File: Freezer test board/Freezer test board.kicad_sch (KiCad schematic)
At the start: 18 parts, among them J1 TB007-508-03BE, J2 TB007-508-03BE, J3 TB007-508-03BE, J4 TB007-508-03BE, J5 TB007-508-03BE, J6 TB007-508-03BE, J7 Conn_02x20_Odd_Even, J8 Conn_02x02_Odd_Even

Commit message: temp commit
I just curved the edges of the PCB and un-did all the connection
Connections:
- no-connect marks 0 -> 5
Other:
- moved on the sheet: H1, H2, H4
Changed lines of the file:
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@@
 		)
+	)
+	(no_connect
+		(at 113.03 78.74)
+	)
+	(no_connect
+		(at 118.11 77.47)
+	)
+	(no_connect
+		(at 107.95 80.01)
+	)
+	(no_connect
+		(at 109.22 77.47)
+	)
+	(no_connect
+		(at 118.11 80.01)
 	)
 	(wire
@@
 	(symbol
 		(lib_id "Mechanical:MountingHole")
-		(at 106.68 38.1 0)
+		(at 106.68 40.64 0)
 		(unit 1)
 		(exclude_from_sim no)
@@
 		(fields_autoplaced yes)
 		(property "Reference" "H4"
-			(at 109.22 36.8299 0)
+			(at 109.22 39.3699 0)
 			(effects
 				(font
@@
 		)
 		(property "Value" "MountingHole"
-			(at 109.22 39.3699 0)
+			(at 109.22 41.9099 0)
 			(effects
 				(font
@@
 		)
 		(property "Footprint" "MountingHole:MountingHole_2.5mm_Pad"
-			(at 106.68 38.1 0)
+			(at 106.68 40.64 0)
 			(effects
 				(font
@@
 		)
 		(property "Datasheet" "~"
-			(at 106.68 38.1 0)
+			(at 106.68 40.64 0)
 			(effects
 				(font
@@
 		)
 		(property "Description" "Mounting Hole without connection"
-			(at 106.68 38.1 0)
+			(at 106.68 40.64 0)
 			(effects
 				(font
@@
 	(symbol
 		(lib_id "Mechanical:MountingHole")
-		(at 85.09 31.75 0)
+		(at 85.09 30.48 0)
 		(unit 1)
 		(exclude_from_sim no)
@@
 		(fields_autoplaced yes)
 		(property "Reference" "H1"
-			(at 87.63 30.4799 0)
+			(at 87.63 29.2099 0)
 			(effects
 				(font
@@
 		)
 		(property "Value" "MountingHole"
-			(at 87.63 33.0199 0)
+			(at 87.63 31.7499 0)
 			(effects
 				(font
@@
 		)
 		(property "Footprint" "MountingHole:MountingHole_2.5mm_Pad"
-			(at 85.09 31.75 0)
+			(at 85.09 30.48 0)
 			(effects
 				(font
@@
 		)
 		(property "Datasheet" "~"
-			(at 85.09 31.75 0)
+			(at 85.09 30.48 0)
 			(effects
 				(font
@@
 		)
 		(property "Description" "Mounting Hole without connection"
-			(at 85.09 31.75 0)
+			(at 85.09 30.48 0)
 			(effects
 				(font
@@
 	(symbol
 		(lib_id "Mechanical:MountingHole")
-		(at 85.09 38.1 0)
+		(at 85.09 41.91 0)
 		(unit 1)
 		(exclude_from_sim no)
@@
 		(fields_autoplaced yes)
 		(property "Reference" "H2"
-			(at 87.63 36.8299 0)
+			(at 87.63 40.6399 0)
 			(effects
 				(font
@@
 		)
 		(property "Value" "MountingHole"
-			(at 87.63 39.3699 0)
+			(at 87.63 43.1799 0)
 			(effects
 				(font
@@
 		)
 		(property "Footprint" "MountingHole:MountingHole_2.5mm_Pad"
-			(at 85.09 38.1 0)
+			(at 85.09 41.91 0)
 			(effects
 				(font
@@
 		)
 		(property "Datasheet" "~"
-			(at 85.09 38.1 0)
+			(at 85.09 41.91 0)
 			(effects
 				(font
@@
 		)
 		(property "Description" "Mounting Hole without connection"
-			(at 85.09 38.1 0)
-			(effects
-				(font
+			(at 85.09 41.91 0)
+			(effects
+				(font

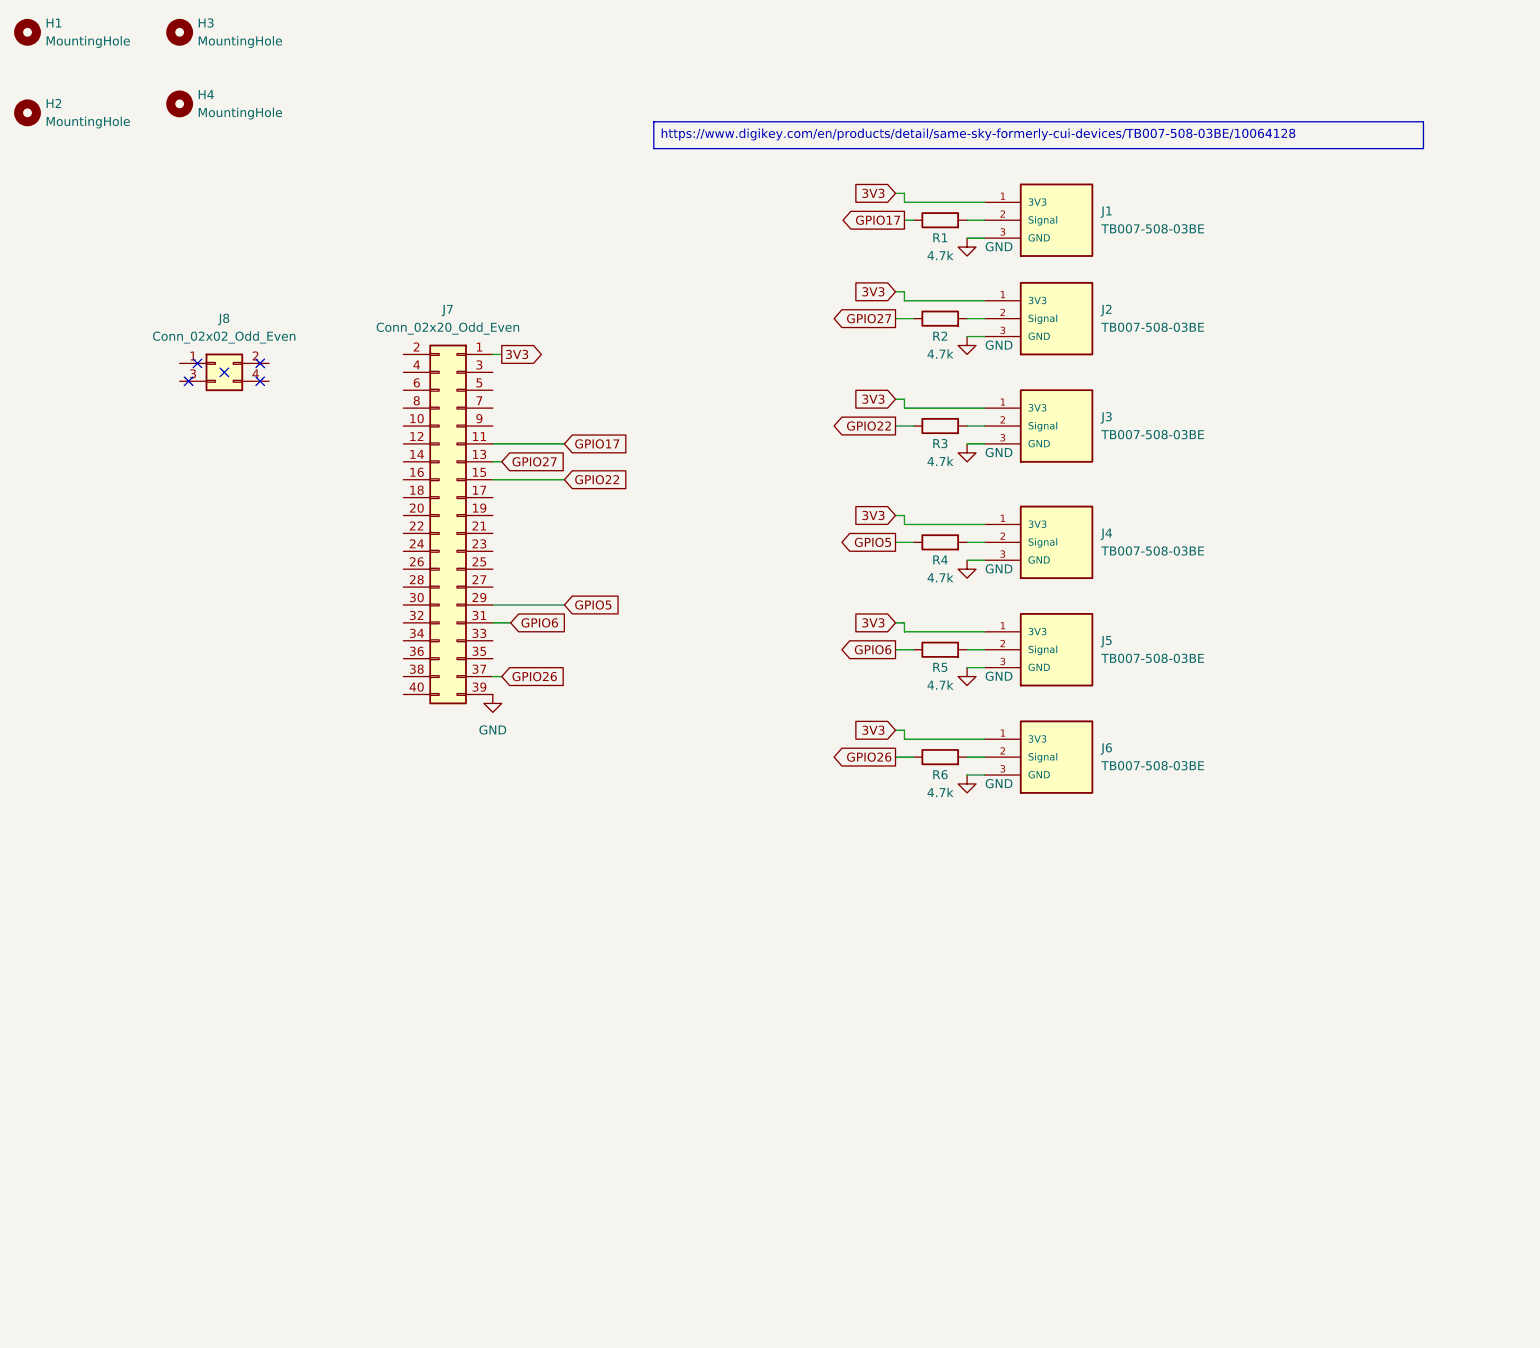
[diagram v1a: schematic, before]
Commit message: Temporary Push
At the moment the most recent changes Made are the following: board has been shrunk by moving the terminal blocks in-between the mounting holes, the terminal blocks have been changed from 5.08mm to 3.54mm. The layers have been changed from SIG-GND-PWR-GND to SIG-GND-PWR-SIG2. Then all of the connections have been removed. No schematic changes
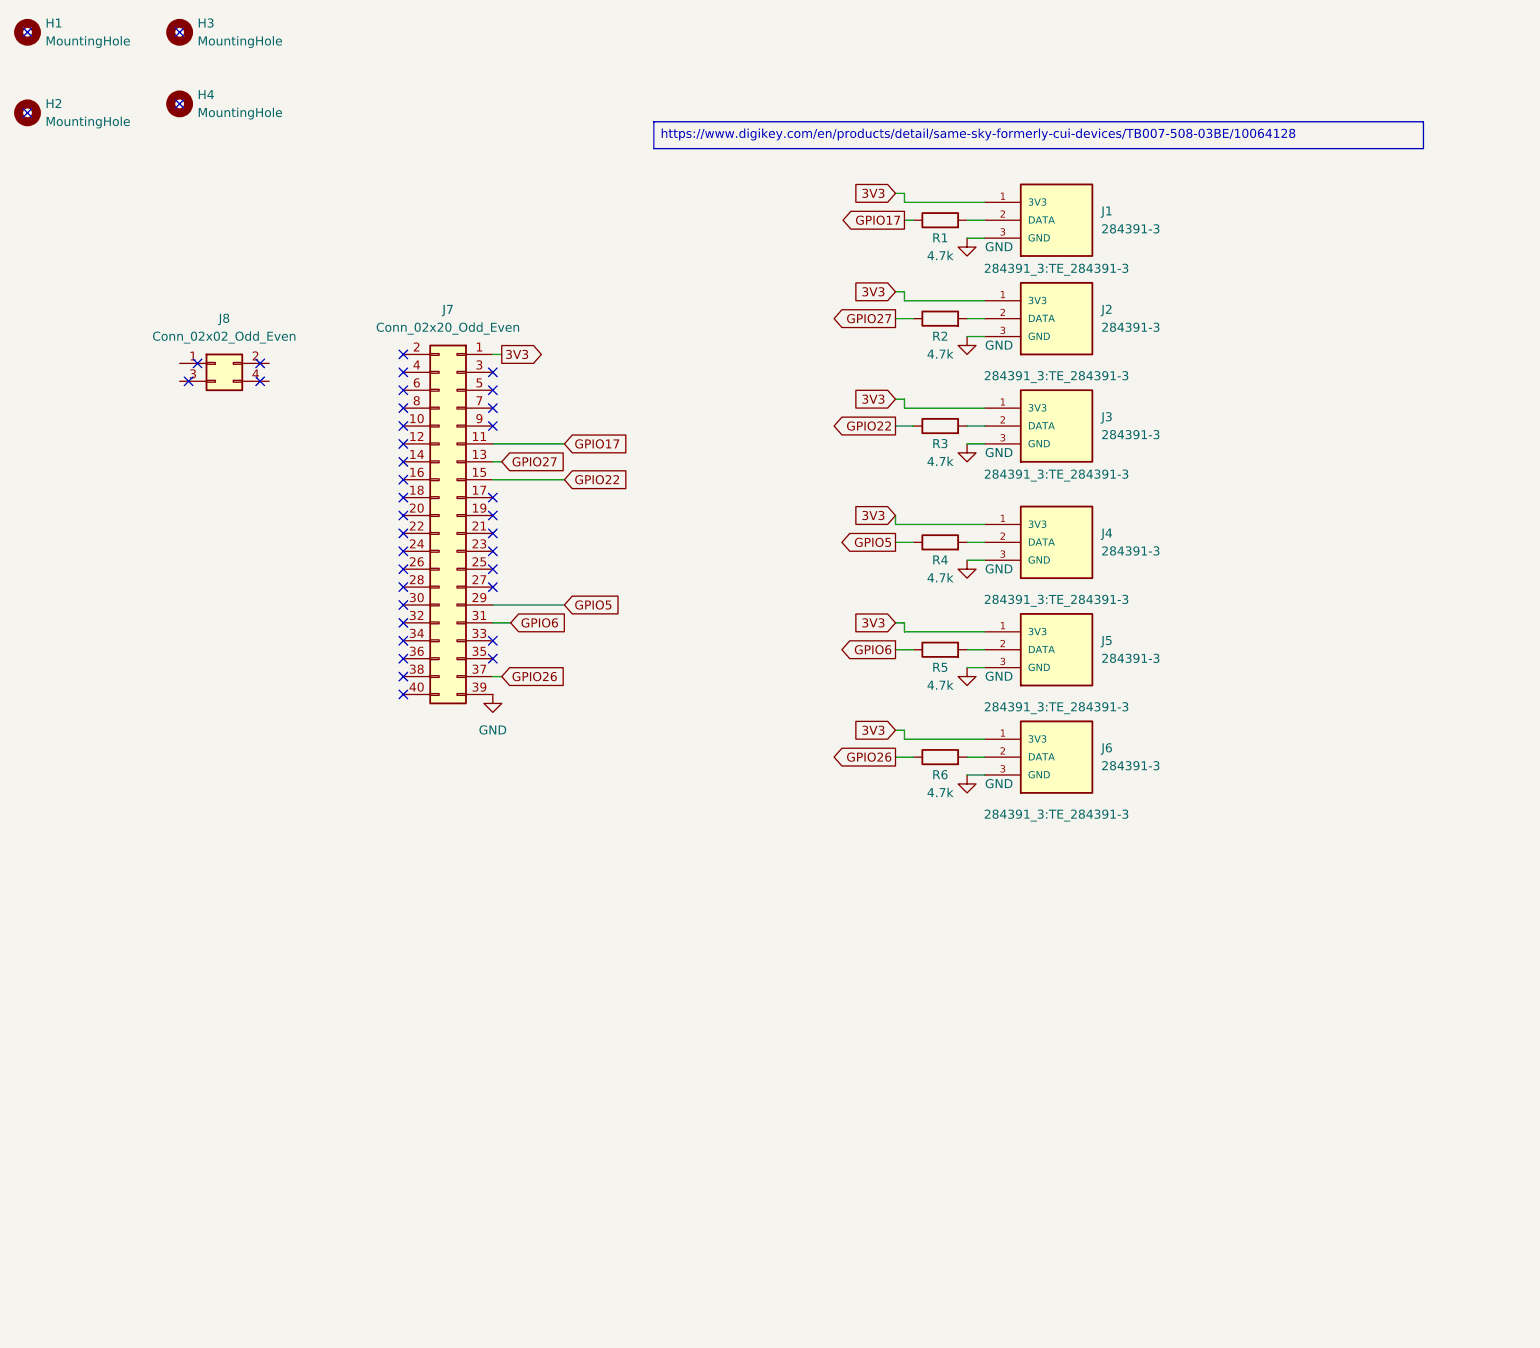
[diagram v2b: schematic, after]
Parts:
- removed J1, J2, J3, J4, J5, J6: TB007-508-03BE, TB007-508-03BE:CUI_TB007-508-03BE, symbol Blockz:TB007-508-03BE
- added J1, J2, J3, J4, J5, J6: 284391-3, 284391_3:TE_284391-3, symbol 284391_3:284391-3
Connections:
- net 3V3: now also J1.1 (3V3), J2.1 (3V3), J3.1 (3V3), J4.1 (3V3), J5.1 (3V3), J6.1 (3V3)
- net GND: now also J1.3 (GND), J2.3 (GND), J3.3 (GND), J4.3 (GND), J5.3 (GND), J6.3 (GND)
- net at R5.2: now also J5.2 (DATA)
- net at R2.2: now also J2.2 (DATA)
- net at R1.2: now also J1.2 (DATA)
- net at R3.2: now also J3.2 (DATA)
- net at R6.2: now also J6.2 (DATA)
- net at R4.2: now also J4.2 (DATA)
- no-connect marks 5 -> 40

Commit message: Uh
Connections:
- no-connect marks 40 -> 36
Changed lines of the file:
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@@
-	)
-	(no_connect
-		(at 106.68 30.48)
 	)
 	(no_connect
@@
 	)
 	(no_connect
-		(at 85.09 30.48)
-	)
-	(no_connect
 		(at 138.43 101.6)
 	)
@@
 	)
 	(no_connect
-		(at 106.68 40.64)
-	)
-	(no_connect
 		(at 151.13 96.52)
 	)
@@
 	)
 	(no_connect
-		(at 85.09 41.91)
-	)
-	(no_connect
 		(at 138.43 121.92)
 	)
@@
 	(wire
 		(pts
+			(xy 152.4 114.3) (xy 151.13 114.3)
+		)
+		(stroke
+			(width 0)
+			(type default)
+		)
+	)
+	(wire
+		(pts
 			(xy 218.44 105.41) (xy 220.98 105.41)
 		)
@@
 		(pts
 			(xy 161.29 93.98) (xy 151.13 93.98)
-		)
-		(stroke
-			(width 0)
-			(type default)
-		)
-	)
-	(wire
-		(pts
-			(xy 153.67 114.3) (xy 151.13 114.3)
 		)
 		(stroke
@@
 		)
 	)
+	(global_label "GPIO6"
+		(shape input)
+		(at 152.4 114.3 0)
+		(fields_autoplaced yes)
+		(effects
+			(font
+				(size 1.27 1.27)
+			)
+			(justify left)
+		)
+		(property "Intersheetrefs" "${INTERSHEET_REFS}"
+			(at 161.07 114.3 0)
+			(effects
+				(font
+					(size 1.27 1.27)
+				)
+				(justify left)
+				(hide yes)
+			)
+		)
+	)
 	(global_label "3V3"
 		(shape output)
@@
 				(hide yes)
 			)
-		)
-	)
-	(global_label "GPIO6"
-		(shape input)
-		(at 153.67 114.3 0)
-		(fields_autoplaced yes)
-		(effects
-			(font
-				(size 1.27 1.27)
-			)
-			(justify left)
-		)
-		(property "Intersheetrefs" "${INTERSHEET_REFS}"
-			(at 162.34 114.3 0)
-			(effects
-				(font
-					(size 1.27 1.27)
-				)
-				(justify left)
-				(hide yes)
-			)

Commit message: changes layouts
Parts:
- removed J1, J2: 284391-3, 284391_3:TE_284391-3, symbol 284391_3:284391-3
- removed R1: 4.7k, Resistor_SMD:R_0201_0603Metric, symbol Device:R
- added J7, J8, J9: 284391-3, 284391_3:TE_284391-3, symbol 284391_3:284391-3
- added R3, R7: 4.7k, Resistor_SMD:R_0201_0603Metric, symbol Device:R
- renumbered J8 to J1, J7 to J2, R3 to R1
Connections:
- net 3V3 is gone; now on net +3V3: J2.1 (pin_1), J3.1 (3V3), J4.1 (3V3), J5.1 (3V3), J6.1 (3V3)
- net GND: now also J7.3 (GND), J8.3 (GND), J9.3 (GND)
- net GPIO17: now also J3.2 (DATA), R1.1
- net GPIO22: now also J5.2 (DATA), R3.1; no longer R1.1
- net GPIO26: now also J8.2 (DATA), J9.2 (DATA), R7.1
- net GPIO27: now also J4.2 (DATA)
- net GPIO5: now also J6.2 (DATA)
- net GPIO6: now also J7.2 (DATA)
- net +3V3: now reaches R2.2
- net +3V3: now also R1.2, R4.2, R5.2, R6.2, J7.1 (3V3), J8.1 (3V3), J9.1 (3V3), R3.2, R7.2
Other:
- moved on the sheet: H2, H3, H4, J3, R1
